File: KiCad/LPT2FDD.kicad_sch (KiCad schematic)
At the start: 2 parts, among them J1 Floppy Connector, J2 LPT Floppy

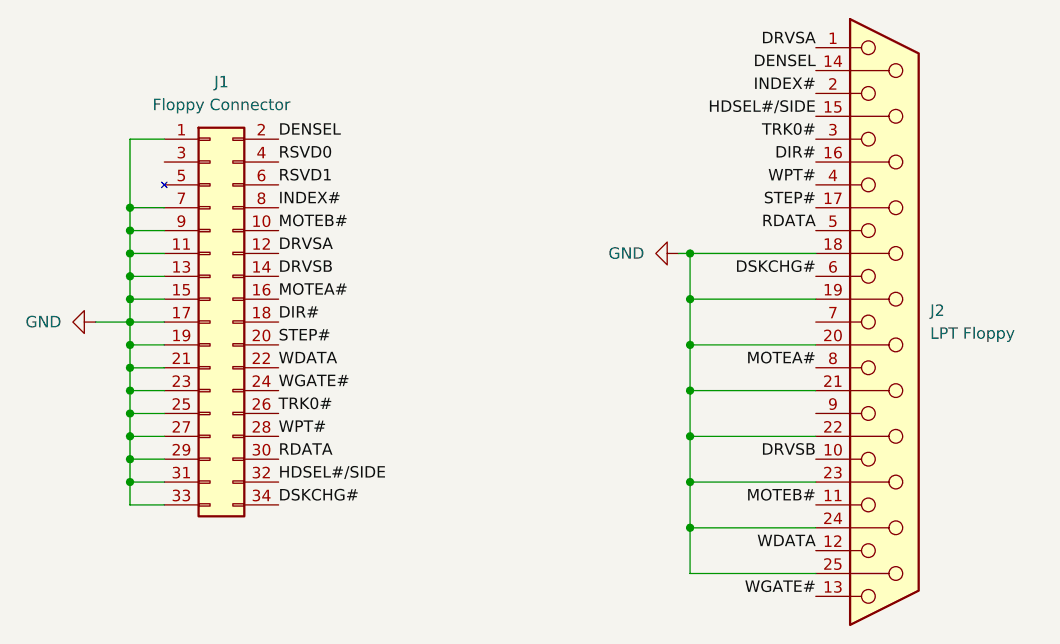
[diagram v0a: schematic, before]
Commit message: v0.5 Add pin 21 and pin 22 jumper for Compaq compatibility
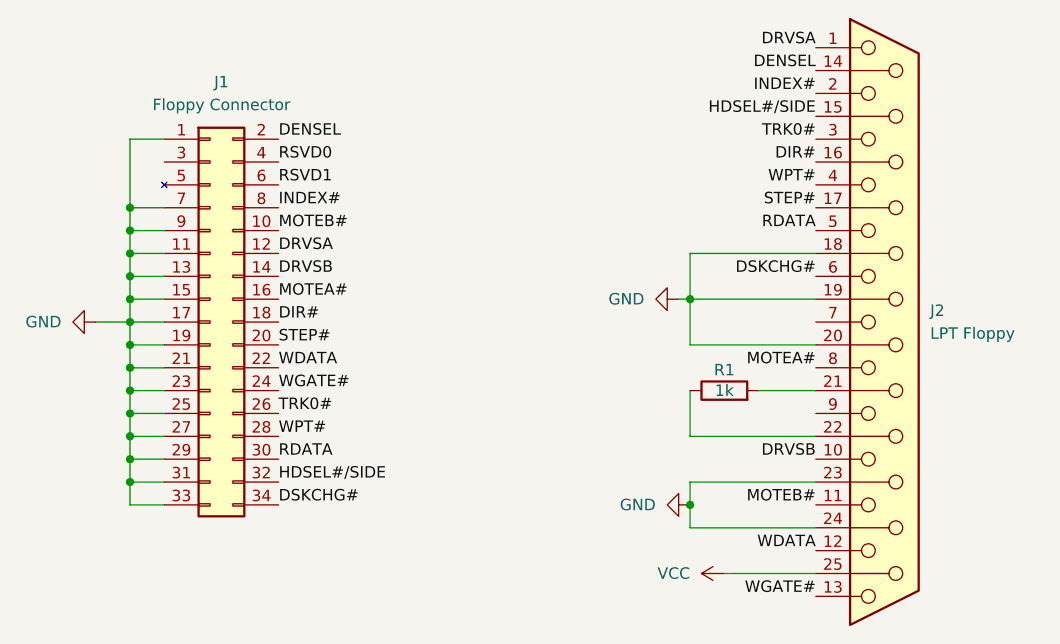
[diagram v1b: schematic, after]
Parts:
- added R1: 1k, Resistor_SMD:R_0805_2012Metric_Pad1.20x1.40mm_HandSolder, symbol Device:R
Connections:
- net GND: no longer J2.21 (P21), J2.22 (P22), J2.25 (P25)
- new net: J2.21 (P21), R1.2
- new net: J2.22 (P22), R1.1
- new net VCC: J2.25 (P25)
